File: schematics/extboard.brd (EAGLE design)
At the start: 45.4 x 54.6 mm, 37 parts, among them X1 FPS009-3000

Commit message: schematics: board rev. A
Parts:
- removed C11, C12, C13, C14: (no value), rcl:E2,5-7
- removed C3, C4, C5, C6, C7, C8: (no value), rcl:C050-035X075
- removed R1: 100k, rcl:0207/10
- removed R10, R11, R12, R13, R14, R15, R16, R17, R18, R19, R20, R8, R9: (no value), rcl:0207/10
- removed X1: FPS009-3000, con-yamaichi:FPS009-3000
- added C15, C16: 0u1, rcl:C050-035X075
- added C18: 2u2, rcl:E2,5-7
- added R21: 250, rcl:0207/10
- added R22: 10, rcl:0207/10
- added SV2, SV3: (no value), con-lstb:MA03-1
- added U$2: LTC1257, ltc1257:DIL-8
- added X2: 1503_02, con-lumberg:1503_02
- added X3: SDBMF, farnell-sd:SDBMF-009XXBXX2
- C10: value (none) -> 2u2
- R2: value 1k -> 250
- R3: value (none) -> 10
- R6, R7: value (none) -> 10k
- moved R7 80.9 mm to (53.3, 52.1), turned to 270 degrees
- moved R6 68.1 mm to (53.3, 38.1), turned to 90 degrees
- moved U$1 31.4 mm to (45.7, 50.8), turned to 180 degrees
- moved C2 24.7 mm to (22.9, 41.9)
- moved C9 22.6 mm to (12.7, 63.5), turned to 270 degrees
- moved R2 21.6 mm to (34.3, 50.8), turned to 180 degrees
- moved SV1 15.2 mm to (3.81, 38.1)
- moved C1 13.1 mm to (22.9, 54.6), turned to 180 degrees
- moved C10 11.5 mm to (34.3, 55.9), turned to 90 degrees
- moved R4 9.25 mm to (15.2, 44.5)
- moved R5 2.84 mm to (17.8, 44.5), turned to 90 degrees
- moved R3 2.84 mm to (25.4, 58.4)
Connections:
- new net N$16: R7.1, SV2.3
- new net N$17: SV2.2, U$1.P$4
- new net N$18: SV3.2, X2.1
- new net N$19: R6.2, U$2.P$4
- new net N$21: C16.1, R21.2, SV3.3
- new net N$22: R21.1, U$2.P$7
- new net N$23: C18.-, R22.2
- net GND: now also C15.2, C16.2, R22.1, R4.2, R5.2, R6.1, R7.2, U$2.P$5, X2.2, X3.3, X3.6; no longer R1.1, X1.3, X1.6
- net N$1: now also U$2.P$1
- net N$10: now also R4.1, X3.9; no longer R4.2, X1.9
- net N$11: now also X3.4; no longer R4.1, R5.1, X1.4
- net N$12: now also X3.1; no longer X1.1
- net N$13: now also X3.2; no longer X1.2
- net N$14: now also X3.5; no longer X1.5
- net N$15: now also X3.7; no longer X1.7
- net N$3: now also U$2.P$3
- net N$4: now also SV2.1, U$2.P$2; no longer R1.2, U$1.P$4
- net N$6: now also C15.1, C18.+, U$2.P$6
- net N$7: now also SV3.1, X2.3
- net N$9: now also R5.1, X3.8; no longer R5.2, X1.8
- net VCC: now also U$2.P$8
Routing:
- net VCC: track 34.3 -> 129.5 mm, vias 0 -> 4
- net N$1: track 13.8 -> 100.1 mm
- net N$3: track 13.8 -> 88.7 mm
- net N$2: track 13.8 -> 76.0 mm
- net GND: track 132.3 -> 185.8 mm, vias 2 -> 4
- net N$7: track 11.4 -> 58.5 mm
- net N$21: track 0.00 -> 44.3 mm
- net N$9: track 22.9 -> 61.5 mm, vias 1 -> 0
- net N$6: track 11.4 -> 49.5 mm
- net N$4: track 6.35 -> 26.8 mm
- net N$24: track 0.00 -> 20.3 mm
- net N$10: track 21.4 -> 40.6 mm, vias 1 -> 0
- net N$12: track 38.6 -> 53.9 mm, vias 1 -> 2
- net N$13: track 39.1 -> 53.9 mm, vias 1 -> 2
- net N$11: track 59.2 -> 72.4 mm
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- added copper zone on layer 1, net N$20
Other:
- board size 45.4 x 54.6 mm -> 60.6 x 66.7 mm
- board text added: "07-2012"
- board text added: "AG Systemtechnische Grundlagen"
- board text added: "HPI"
- board text added: "Hasso-Plattner-Instutut"
- board text added: "Rev. A"
- board text added: "SD&DAC Extension Board"
- board text added: "für Softwaresystemtechnik GmbH"

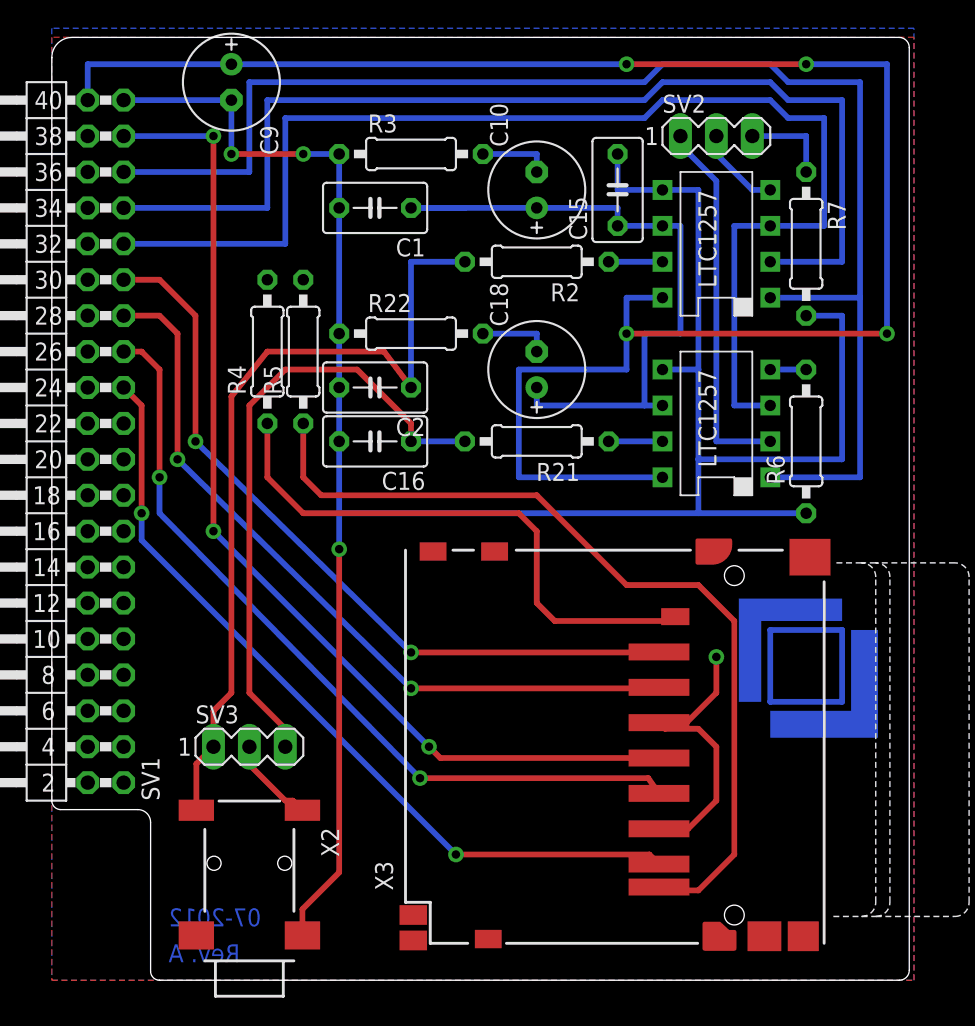
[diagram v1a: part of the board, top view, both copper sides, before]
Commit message: schematics: Fix in Rev A
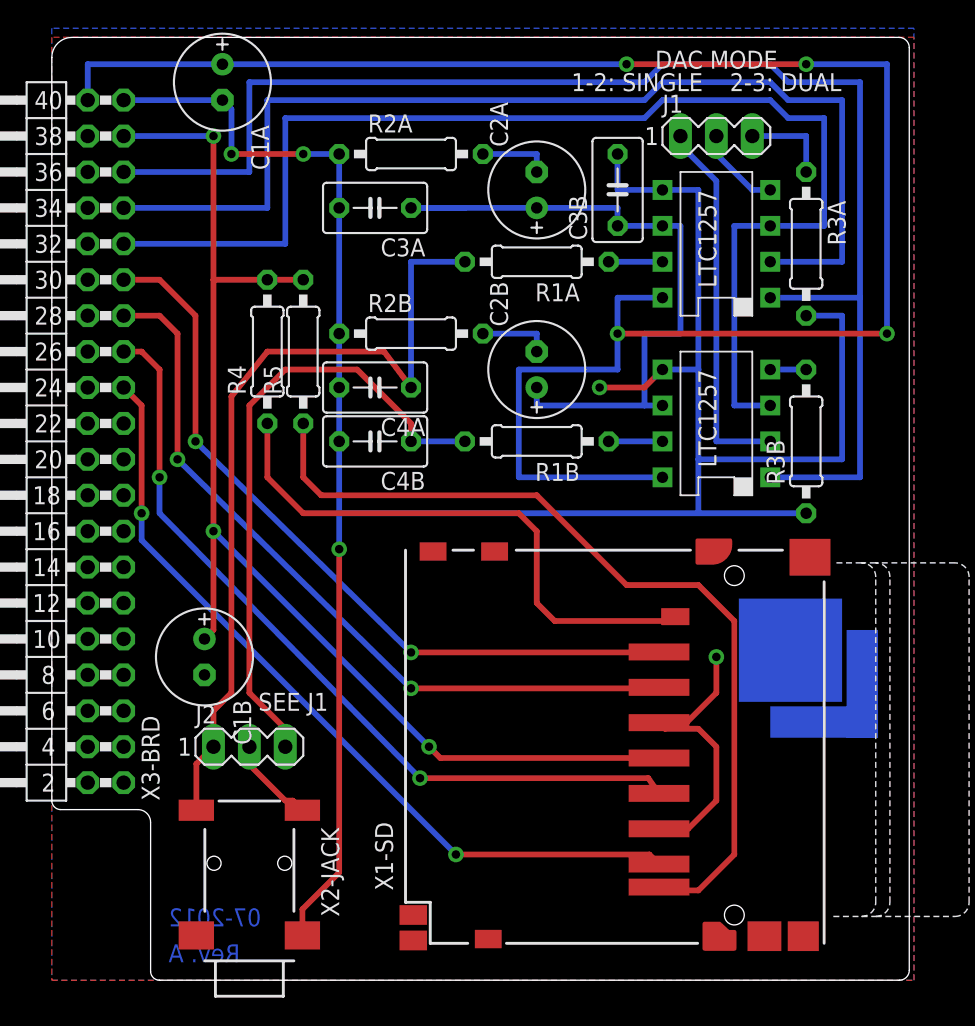
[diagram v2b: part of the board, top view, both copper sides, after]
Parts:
- removed C9: 2u2, rcl:E2,5-7
- added C1A, C1B: 2u2, rcl:E2,5-7
- X1-SD: value SDBMF -> (none)
- renumbered C1 to C3A, C10 to C2A, C15 to C3B, C16 to C4B, C18 to C2B, C2 to C4A, R2 to R1A, R21 to R1B, R22 to R2B, R3 to R2A, R6 to R3B, R7 to R3A, SV1 to X3-BRD, SV2 to J1, SV3 to J2, U$1 to U1, U$2 to U2, X2 to X2-JACK, X3 to X1-SD
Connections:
- net GND: now also C1A.-, C1B.-; no longer C9.-, R4.2, R5.2
- net N$11: now also C1B.+, R4.2, R5.2
- net VCC: now also C1A.+; no longer C9.+
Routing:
- net N$24: track 20.3 -> 0.00 mm
- net N$11: track 72.4 -> 86.7 mm
- net GND: track 185.8 -> 190.4 mm, vias 4 -> 5
- net VCC: track 129.5 -> 130.2 mm
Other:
- board text added: "1-2: SINGLE"
- board text added: "2-3: DUAL"
- board text added: "DAC MODE"
- board text added: "SEE J1"

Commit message: schematics: next iteration
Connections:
- new net N$24: X1-SD.SW1, X3-BRD.34
- new net N$25: X1-SD.SW2, X3-BRD.36
- new net N$26: X1-SD.SW3, X3-BRD.38
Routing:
- net N$25: track 0.00 -> 97.0 mm, vias 0 -> 3
- net N$26: track 0.00 -> 70.6 mm, vias 0 -> 3
- net N$24: track 0.00 -> 65.8 mm, vias 0 -> 3
- net GND: track 190.4 -> 185.2 mm
- net N$12: track 53.9 -> 55.4 mm
- net N$13: track 53.9 -> 55.0 mm
- net N$15: track 57.4 -> 58.5 mm
- net N$10: track 40.6 -> 39.5 mm
- net N$11: track 86.7 -> 85.8 mm, vias 3 -> 4
- net N$9: track 61.5 -> 60.7 mm

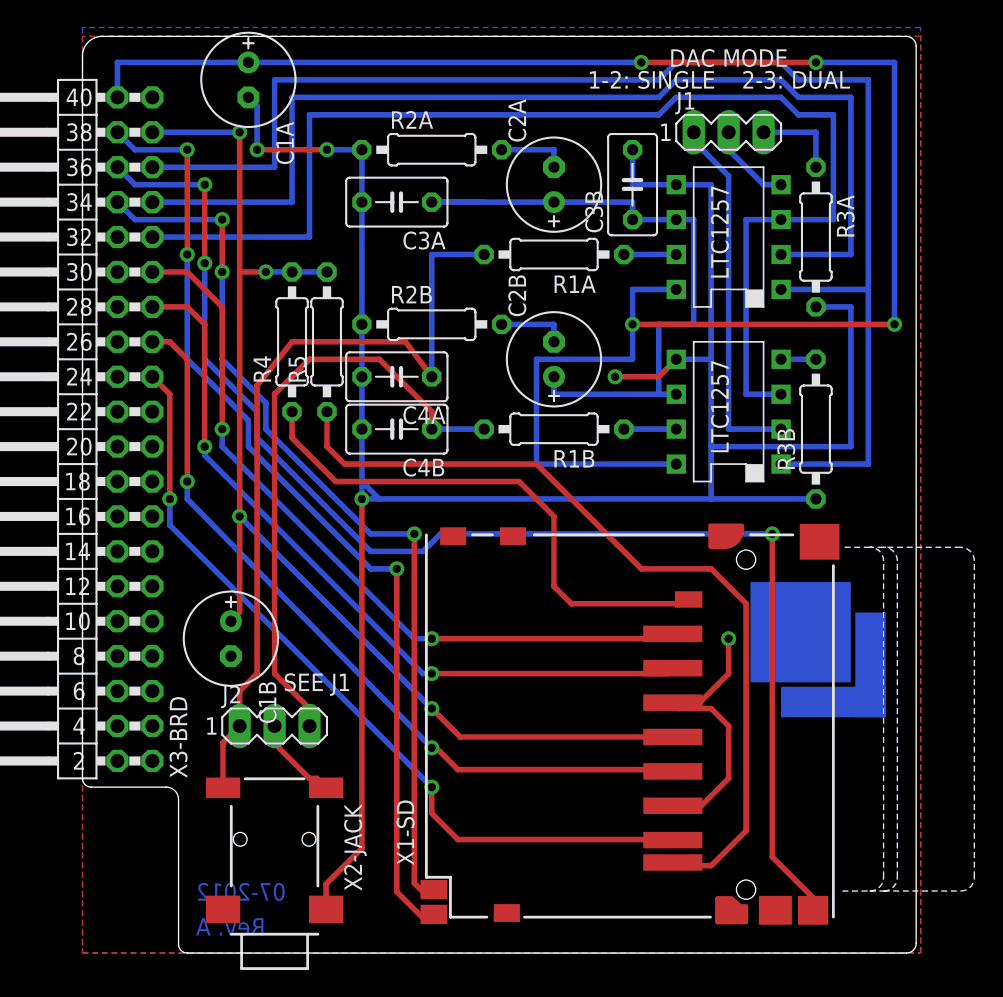
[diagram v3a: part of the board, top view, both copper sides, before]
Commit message: schematic: Revision A iteration - jumpers for connecting DATA2 and DATA3 to board
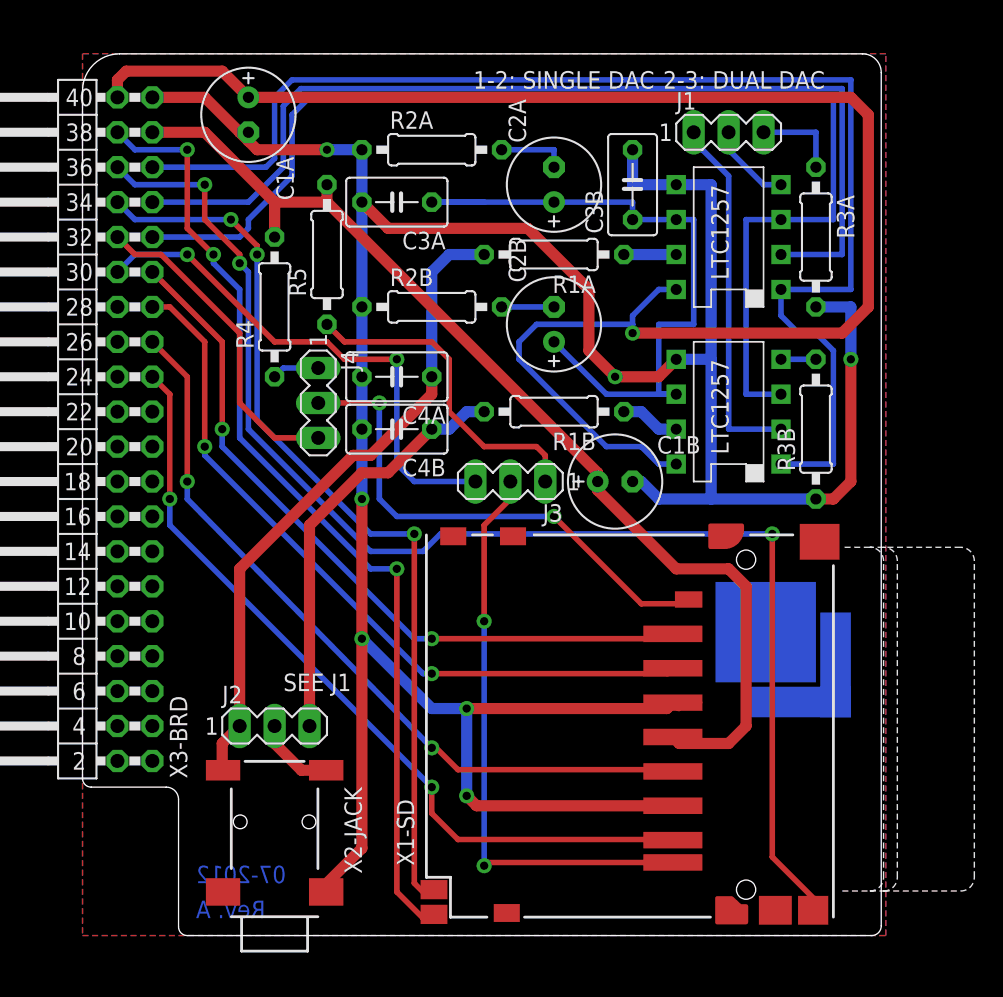
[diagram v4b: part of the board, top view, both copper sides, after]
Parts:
- added J3, J4: (no value), con-lstb:MA03-1
- moved C1B 30.2 mm to (38.7, 34.3), turned to 0 degrees
- moved R5 6.35 mm to (17.8, 50.8)
- moved R4 2.84 mm to (14.0, 47.0)
- moved C1A 2.54 mm to (12.1, 61.0)
- moved C2B 2.54 mm to (34.3, 45.7)
- moved R2B 1.27 mm to (25.4, 47.0)
- moved X2-JACK 1.27 mm to (14.0, 2.54)
- moved R1B 1.27 mm to (34.3, 39.4)
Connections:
- removed net N$9 (its old number): R5.1, X1-SD.8
- new net N$27: J4.1, R4.1
- new net N$28: J3.2, X1-SD.8
- new net N$29: J4.2, X1-SD.9
- new net N$30: J4.3, X3-BRD.32
- new net N$31: J3.3, X3-BRD.30
- net N$10: now also J3.1, R5.1; no longer R4.1, X1-SD.9
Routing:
- net N$9 (its old number): track 60.7 -> 0.00 mm
- net N$28: track 0.00 -> 42.6 mm, vias 0 -> 2
- net N$31: track 0.00 -> 37.9 mm, vias 0 -> 2
- net N$29: track 0.00 -> 37.2 mm, vias 0 -> 2
- net GND: track 185.2 -> 219.3 mm, vias 5 -> 7
- net N$30: track 0.00 -> 23.6 mm
- net N$10: track 39.5 -> 24.0 mm
- net N$21: track 44.3 -> 30.7 mm
- net VCC: track 130.2 -> 119.2 mm, vias 4 -> 1
- net N$7: track 58.5 -> 47.7 mm
- net N$9: track 85.8 -> 77.6 mm, vias 4 -> 0
- net N$1: track 100.1 -> 95.2 mm
- net N$27: track 0.00 -> 3.44 mm
- net N$2: track 76.0 -> 72.7 mm
- net N$6: track 49.5 -> 51.1 mm
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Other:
- board size 60.6 x 66.7 mm -> 58.1 x 64.1 mm
- board text added: "1-2: SINGLE DAC"
- board text added: "2-3: DUAL DAC"
- board text removed: "1-2: SINGLE"
- board text removed: "2-3: DUAL"
- board text removed: "DAC MODE"
